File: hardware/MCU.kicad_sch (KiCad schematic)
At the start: 0 parts

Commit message: Completed display schematic
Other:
- sheet User Interface ports: added DISPLAY_BACKLIGHT_EN, Display_COMIN, Display_CS, Display_MOSI, Display_SCK; removed none
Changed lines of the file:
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@@
 		)
 		(fill
-			(color 0 0 0 0)
+			(color 194 194 0 0.5019607843)
 		)
 		(property "Sheetname" "User Interface"
@@
 			)
 		)
+		(pin "DISPLAY_BACKLIGHT_EN" input
+			(at 66.675 46.99 0)
+			(effects
+				(font
+					(size 1.524 1.524)
+				)
+				(justify right)
+			)
+		)
+		(pin "Display_COMIN" input
+			(at 66.675 44.45 0)
+			(effects
+				(font
+					(size 1.524 1.524)
+				)
+				(justify right)
+			)
+		)
+		(pin "Display_CS" input
+			(at 66.675 34.29 0)
+			(effects
+				(font
+					(size 1.524 1.524)
+				)
+				(justify right)
+			)
+		)
+		(pin "Display_MOSI" input
+			(at 66.675 29.21 0)
+			(effects
+				(font
+					(size 1.524 1.524)
+				)
+				(justify right)
+			)
+		)
+		(pin "Display_SCK" input
+			(at 66.675 31.75 0)
+			(effects
+				(font
+					(size 1.524 1.524)
+				)
+				(justify right)
+			)
+		)

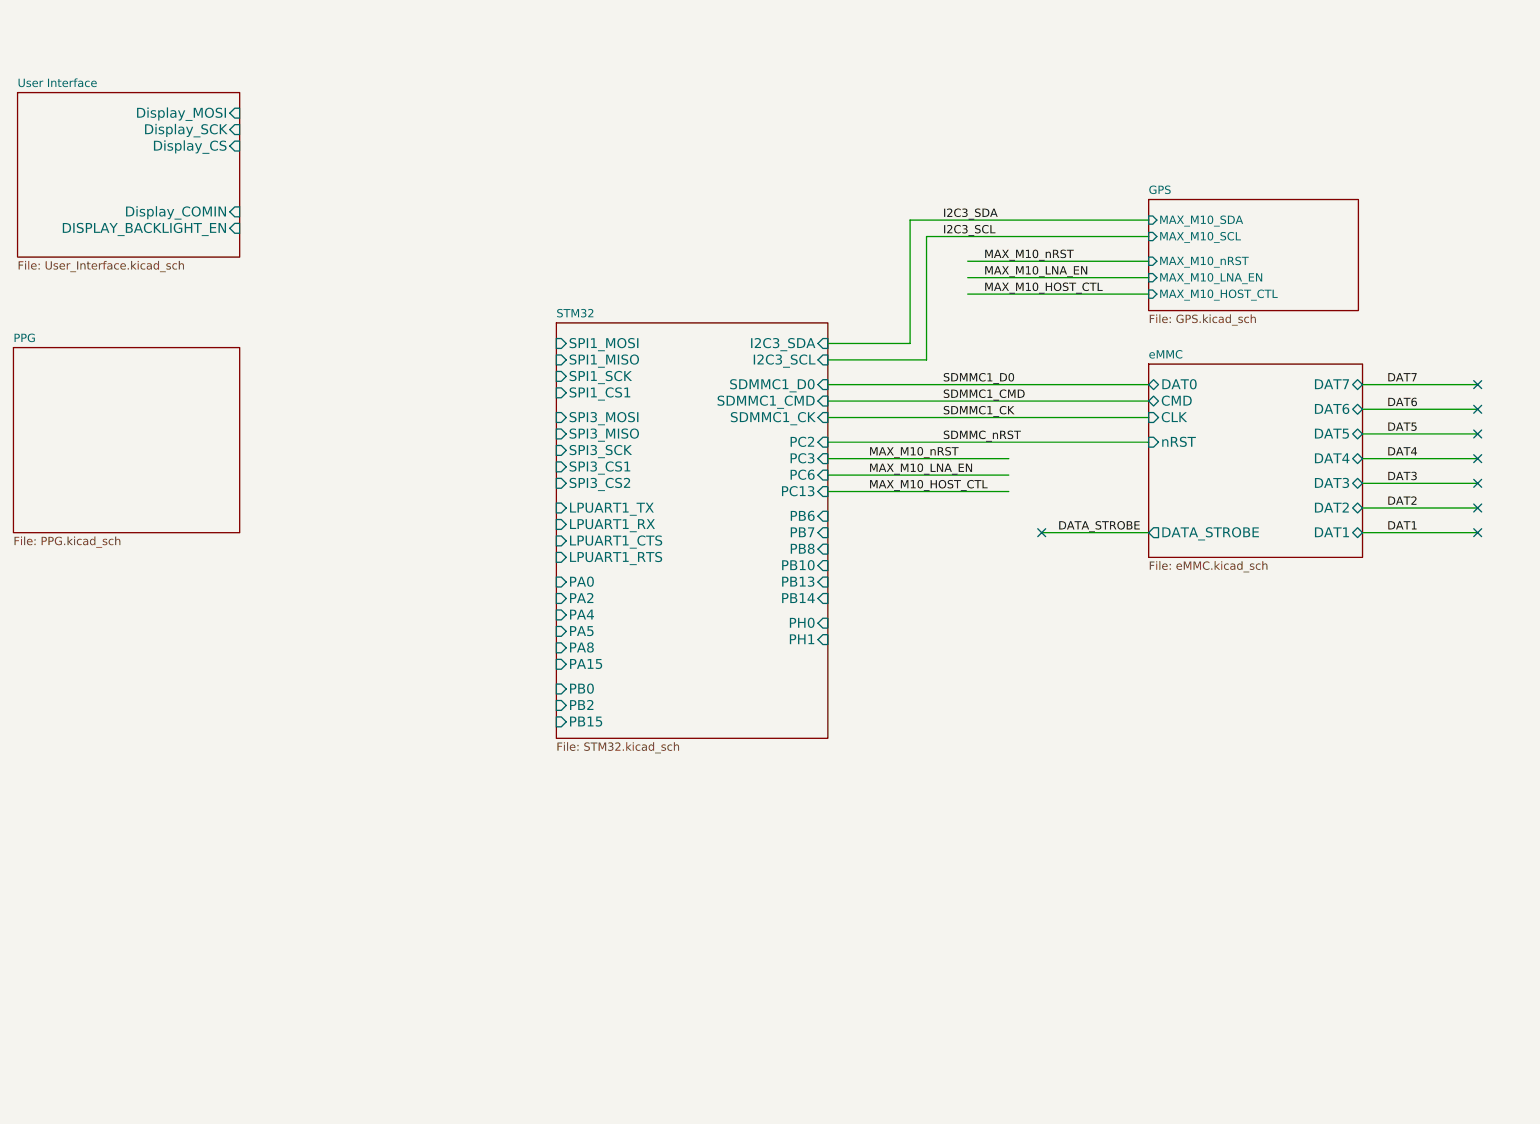
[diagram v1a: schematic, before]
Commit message: Added bluetooth module schematic and environmental perception block"
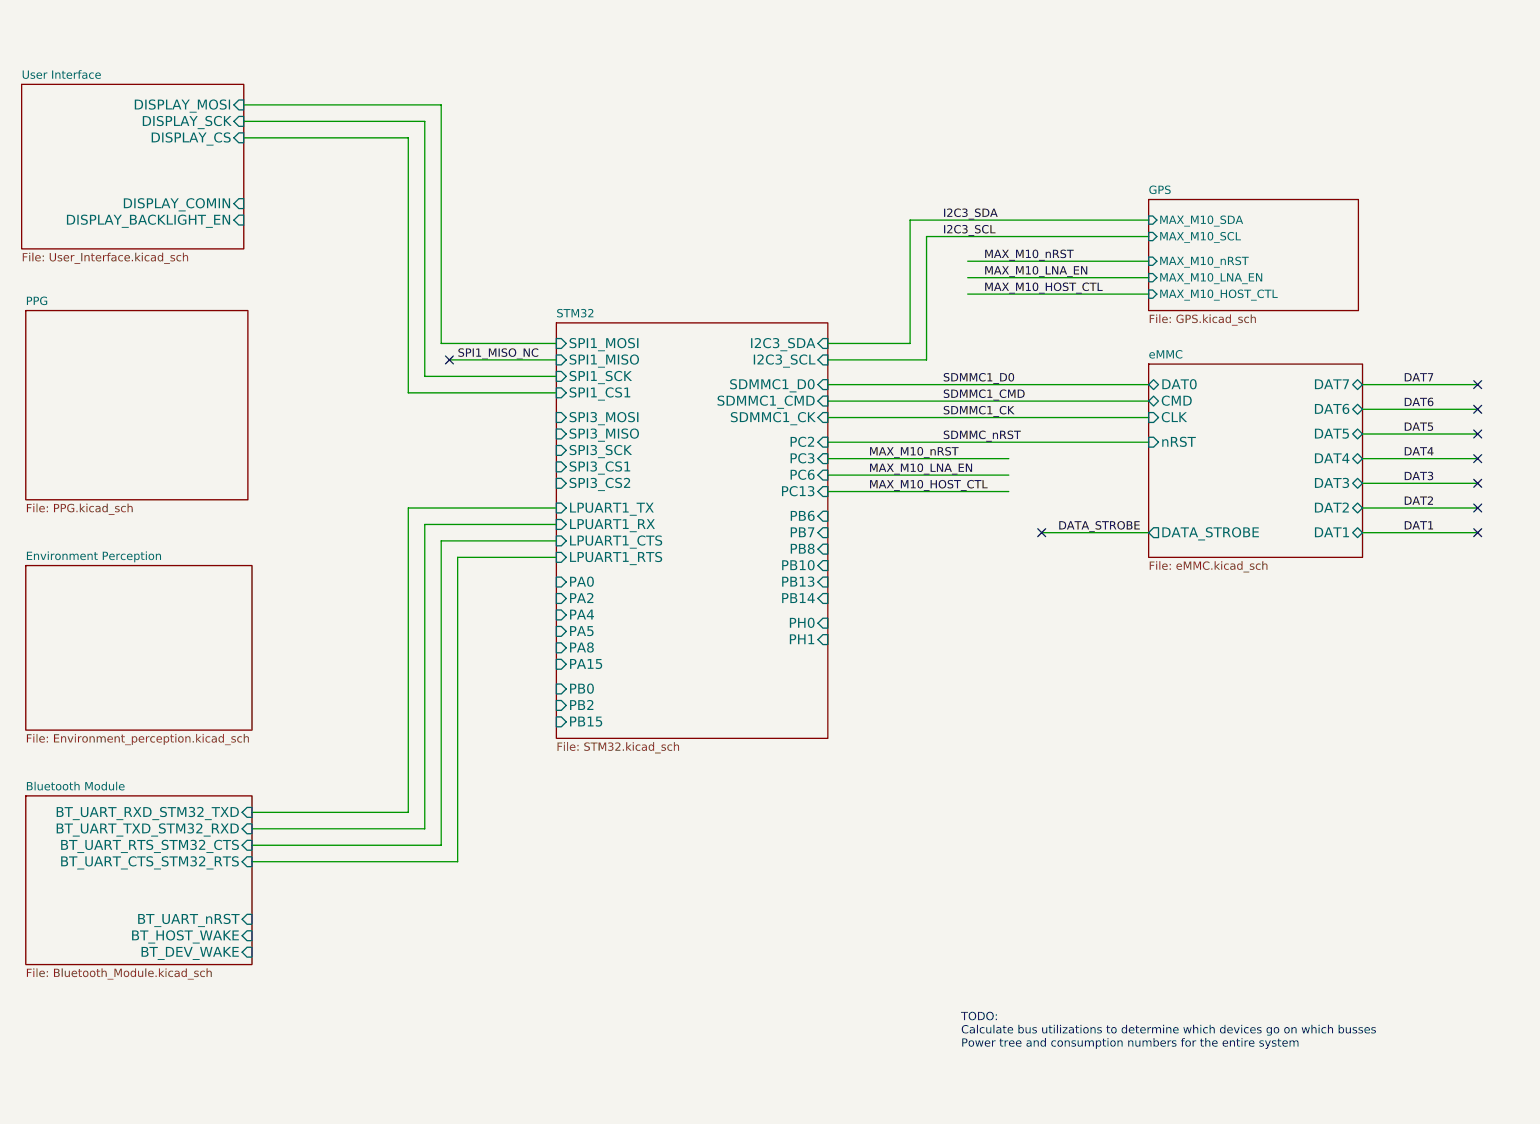
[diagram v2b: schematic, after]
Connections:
- no-connect marks 8 -> 9
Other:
- added sheet Bluetooth Module (Bluetooth_Module.kicad_sch)
- added sheet Environment Perception (Environment_perception.kicad_sch)
- sheet User Interface ports: added DISPLAY_COMIN, DISPLAY_CS, DISPLAY_MOSI, DISPLAY_SCK; removed Display_COMIN, Display_CS, Display_MOSI, Display_SCK
- note added: "TODO: Calculate bus utilizations to determine which devices go on which busses Power tree and consumption numbers for the entire system"

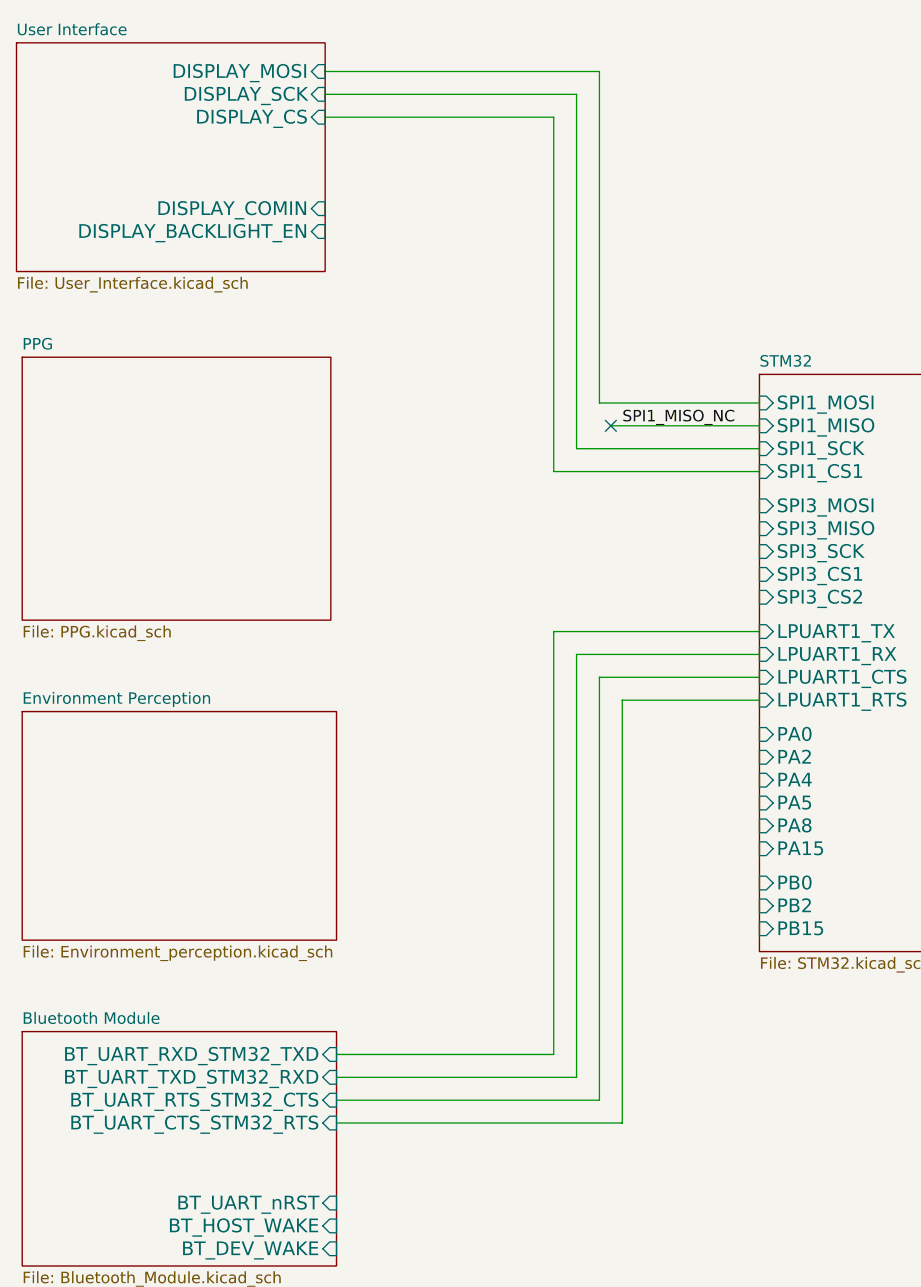
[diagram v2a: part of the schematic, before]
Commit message: Added IMU and barometer, and connected to STM32
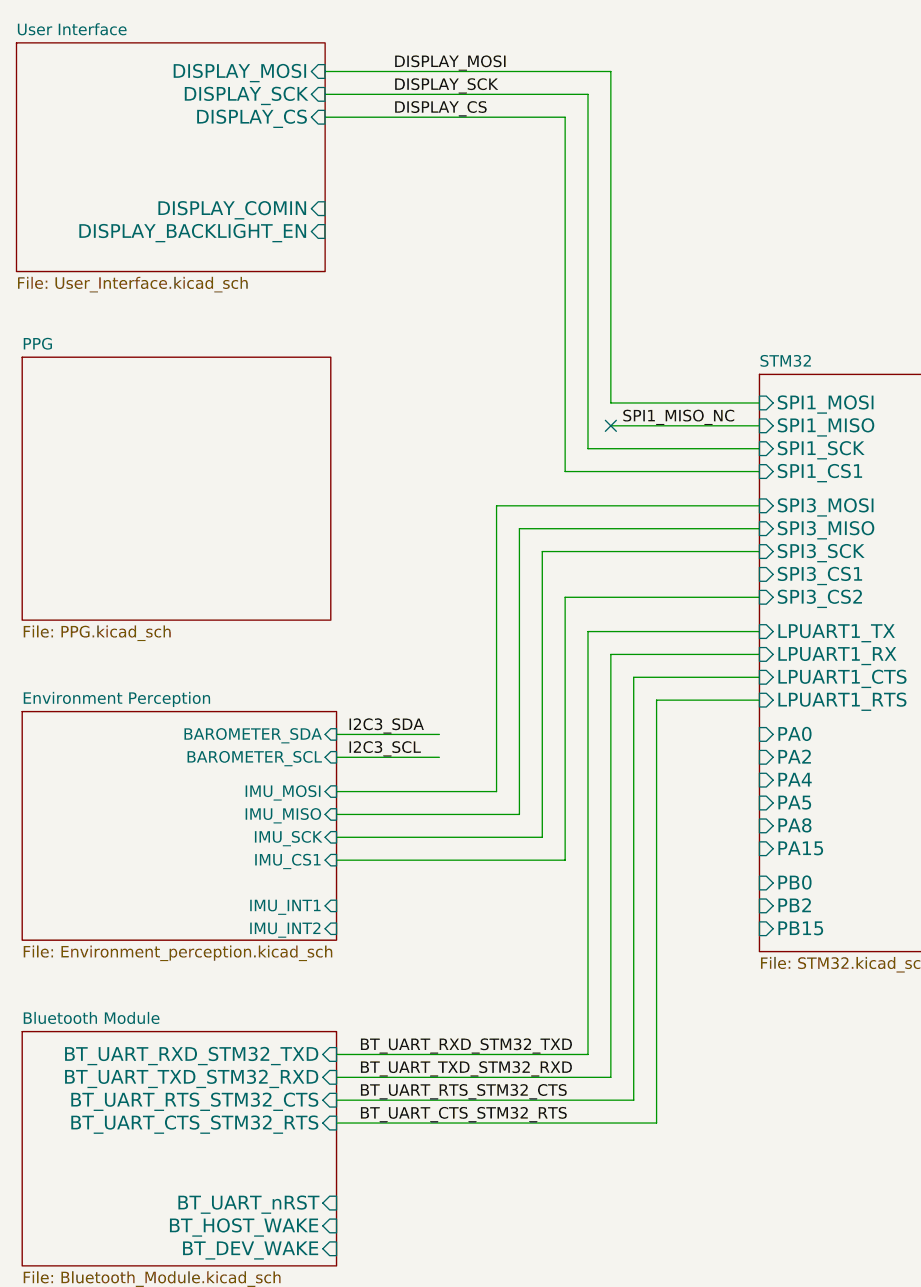
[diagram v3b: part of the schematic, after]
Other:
- sheet Environment Perception ports: added BAROMETER_SCL, BAROMETER_SDA, IMU_CS1, IMU_INT1, IMU_INT2, IMU_MISO, IMU_MOSI, IMU_SCK; removed none

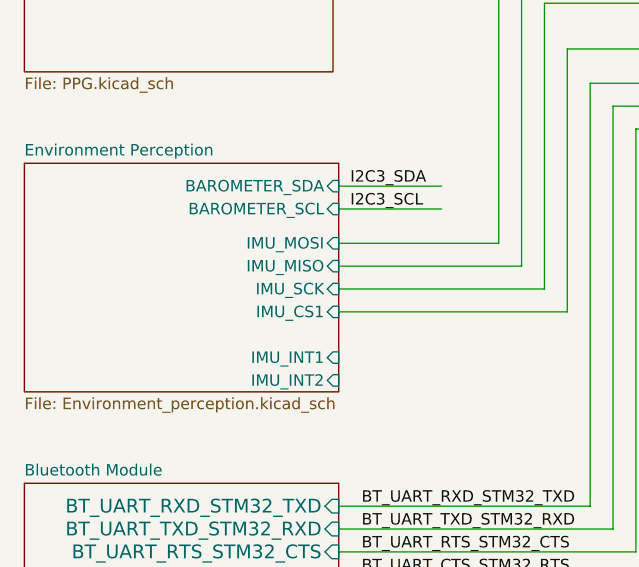
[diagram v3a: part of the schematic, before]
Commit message: Updated IMU to BMI270 for supply chain reason
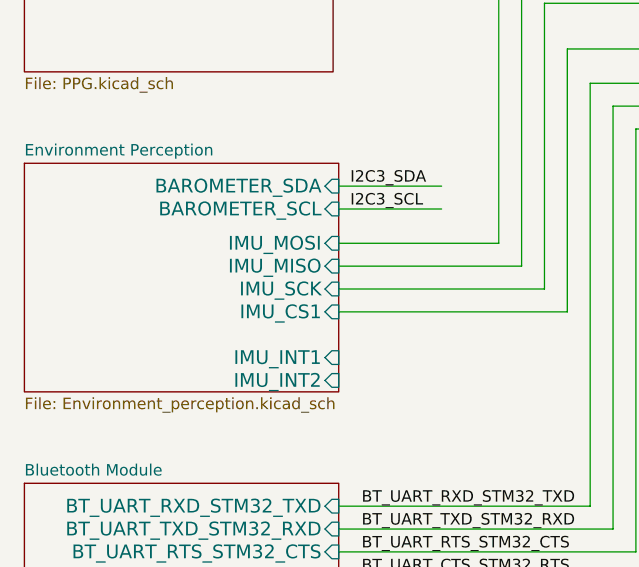
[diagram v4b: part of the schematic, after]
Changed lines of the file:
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@@
 			(effects
 				(font
-					(size 1.27 1.27)
+					(size 1.524 1.524)
 				)
 				(justify right)
@@
 			(effects
 				(font
-					(size 1.27 1.27)
+					(size 1.524 1.524)
 				)
 				(justify right)
@@
 			(effects
 				(font
-					(size 1.27 1.27)
+					(size 1.524 1.524)
 				)
 				(justify right)
@@
 			(effects
 				(font
-					(size 1.27 1.27)
+					(size 1.524 1.524)
 				)
 				(justify right)
@@
 			(effects
 				(font
-					(size 1.27 1.27)
+					(size 1.524 1.524)
 				)
 				(justify right)
@@
 			(effects
 				(font
-					(size 1.27 1.27)
+					(size 1.524 1.524)
 				)
 				(justify right)
@@
 			(effects
 				(font
-					(size 1.27 1.27)
+					(size 1.524 1.524)
 				)
 				(justify right)
@@
 			(effects
 				(font
-					(size 1.27 1.27)
+					(size 1.524 1.524)
 				)
 				(justify right)

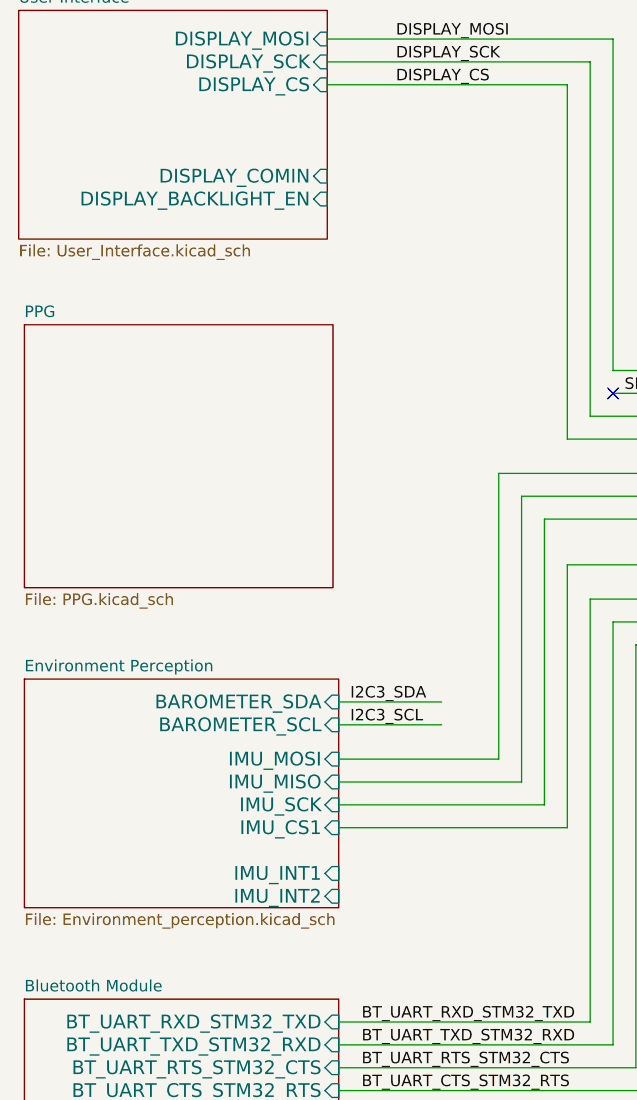
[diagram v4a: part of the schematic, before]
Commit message: Changing barometer, STM32 and power rails
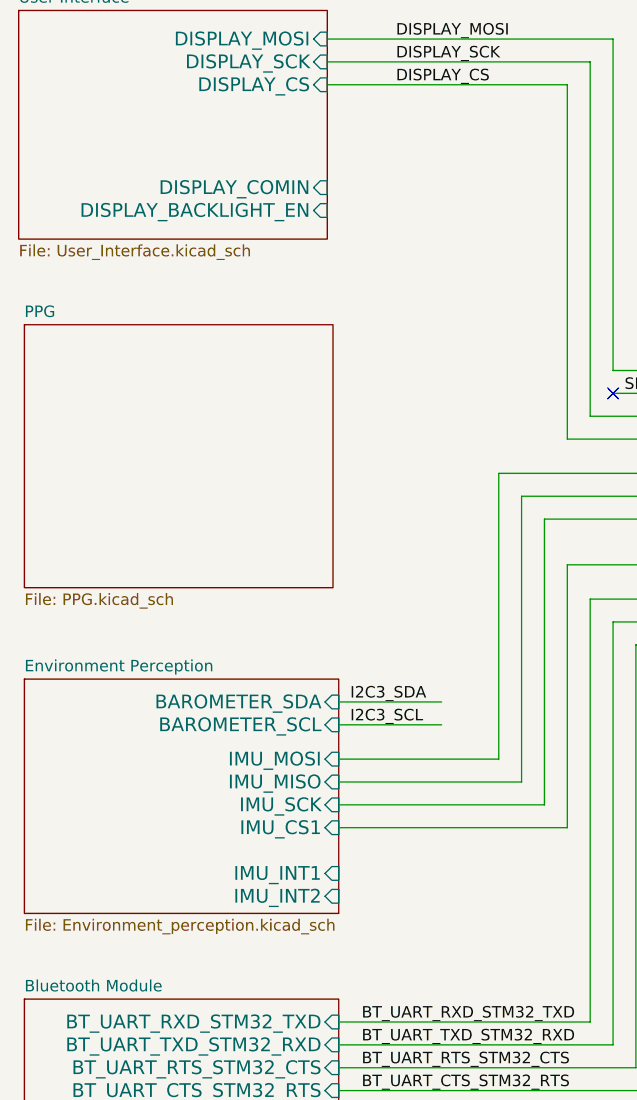
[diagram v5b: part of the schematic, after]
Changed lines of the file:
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@@
 	(sheet
 		(at 33.655 99.06)
-		(size 34.925 25.4)
+		(size 34.925 26.035)
 		(exclude_from_sim no)
 		(in_bom yes)
@@
 		)
 		(property "Sheetfile" "Environment_perception.kicad_sch"
-			(at 33.655 125.0446 0)
+			(at 33.655 125.6796 0)
 			(show_name no)
 			(do_not_autoplace no)
@@
 		)
 		(pin "DISPLAY_COMIN" input
-			(at 67.31 43.18 0)
+			(at 67.31 44.45 0)
 			(effects
 				(font
@@
 		)
 		(pin "DISPLAY_BACKLIGHT_EN" input
-			(at 67.31 45.72 0)
-			(effects
-				(font
+			(at 67.31 46.99 0)
+			(effects
+				(font

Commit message: Added AFE SNR study!
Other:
- note added: "TODO: Calculate bus utilizations to determine which devices go on which busses Power tree and consumption numbers for the entire system Goals for today: 1. Update STM32 to STM32U5A5QJI3Q 2. Choose PPG AFE and complete that schematic 2a. VDDIO2 to 3p3 for display 2b. What are the wavelengths that we care about 2c. Trade study for LEDs/VCSELs 3. Update barometer to Bosch part 4. Power supplies"
- note removed: "TODO: Calculate bus utilizations to determine which devices go on which busses Power tree and consumption numbers for the entire system"
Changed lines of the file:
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@@
 	(generator_version "10.0")
 	(paper "A4")
-	(text "TODO:\nCalculate bus utilizations to determine which devices go on which busses\nPower tree and consumption numbers for the entire system"
+	(text "TODO:\nCalculate bus utilizations to determine which devices go on which busses\nPower tree and consumption numbers for the entire system\n\nGoals for today:\n1. Update STM32 to STM32U5A5QJI3Q\n2. Choose PPG AFE and complete that schematic\n2a. VDDIO2 to 3p3 for display\n2b. What are the wavelengths that we care about\n2c. Trade study for LEDs/VCSELs\n3. Update barometer to Bosch part\n4. Power supplies"
 		(exclude_from_sim no)
 		(at 178.054 170.942 0)
